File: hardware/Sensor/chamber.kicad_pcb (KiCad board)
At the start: 2 copper layers, 100 x 100 mm, 100 parts, among them J1 USB_B_Micro, J32 RF_Shield_Two_Pieces, J33 RF_Shield_Two_Pieces, J34 Conn_Coaxial, J51 Conn_02x05_Counter_Clockwise, J52 Conn_01x04, Q31 BC859, Q32 Q_NMOS_GDS, Q51 2N7002, Q52 Q_NPN_BEC, SW31 SW_DPDT_x2, SW32 SW_DPDT_x2, U31 MC34063AD, U32 LMC662, U33 LM358, U51 Opamp_Dual_Generic, U52 MCP3425A0T-ECH, U53 MCP3425A0T-ECH, U54 STM8S003F3P

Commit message: fix #64
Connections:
- J52 pad 2: /DataAcquisition/TX -> /DataAcquisition/RX
- J52 pad 3: /DataAcquisition/RX -> /DataAcquisition/TX
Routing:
- net /DataAcquisition/RX: track 14.9 -> 12.7 mm
- net /DataAcquisition/TX: track 9.60 -> 11.4 mm
- net /DataAcquisition/INT0: track 37.9 -> 37.0 mm
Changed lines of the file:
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@@
     (thickness 1.6)
     (drawings 19)
-    (tracks 665)
+    (tracks 668)
     (zones 0)
     (modules 100)
@@
   )
   (setup
-    (last_trace_width 0.3048)
+    (last_trace_width 0.254)
     (user_trace_width 0.254)
     (trace_clearance 0.254)
@@
       (net 1 GND))
     (pad 3 thru_hole oval (at 0 5.08 90) (size 1.7 1.7) (drill 1) (layers *.Cu *.Mask)
-      (net 47 /DataAcquisition/RX))
-    (pad 2 thru_hole oval (at 0 2.54 90) (size 1.7 1.7) (drill 1) (layers *.Cu *.Mask)
       (net 48 /DataAcquisition/TX))
+    (pad 2 thru_hole oval (at 0 2.54 90) (size 1.7 1.7) (drill 1) (layers *.Cu *.Mask)
+      (net 47 /DataAcquisition/RX))
     (pad 1 thru_hole rect (at 0 0 90) (size 1.7 1.7) (drill 1) (layers *.Cu *.Mask))
     (model ${KISYS3DMOD}/Connector_PinSocket_2.54mm.3dshapes/PinSocket_1x04_P2.54mm_Horizontal.wrl
@@
   (segment (start 126.286 134.331) (end 126.206 134.251) (width 0.3048) (layer F.Cu) (net 41) (status 30))
   (segment (start 130.466 134.331) (end 126.286 134.331) (width 0.3048) (layer F.Cu) (net 41) (status 30))
-  (segment (start 200.064001 135.993999) (end 200.914 135.144) (width 0.3048) (layer F.Cu) (net 42))
   (segment (start 184.0078 131.181) (end 184.767598 131.940798) (width 0.3048) (layer F.Cu) (net 42))
-  (segment (start 198.898 137.16) (end 200.064001 135.993999) (width 0.3048) (layer F.Cu) (net 42))
-  (segment (start 184.767598 131.940798) (end 184.767598 136.071074) (width 0.3048) (layer F.Cu) (net 42))
   (segment (start 182.978 131.181) (end 184.0078 131.181) (width 0.3048) (layer F.Cu) (net 42))
+  (segment (start 184.767598 131.940798) (end 184.767598 136.071074) (width 0.3048) (layer F.Cu) (net 42))
   (segment (start 184.767598 136.071074) (end 185.856524 137.16) (width 0.3048) (layer F.Cu) (net 42))
+  (segment (start 200.064001 135.993999) (end 200.914 135.144) (width 0.3048) (layer F.Cu) (net 42))
   (segment (start 185.856524 137.16) (end 198.898 137.16) (width 0.3048) (layer F.Cu) (net 42))
+  (segment (start 198.898 137.16) (end 200.064001 135.993999) (width 0.3048) (layer F.Cu) (net 42))
   (segment (start 197.2192 135.144) (end 198.374 135.144) (width 0.3048) (layer F.Cu) (net 43) (status 20))
   (segment (start 195.58 135.645) (end 196.587 135.645) (width 0.3048) (layer F.Cu) (net 43))
   (segment (start 197.088 135.144) (end 197.2192 135.144) (width 0.3048) (layer F.Cu) (net 43))
   (segment (start 196.587 135.645) (end 197.088 135.144) (width 0.3048) (layer F.Cu) (net 43))
-  (segment (start 194.265 136.16) (end 194.78 135.645) (width 0.3048) (layer F.Cu) (net 43))
-  (segment (start 189.992 136.16) (end 194.265 136.16) (width 0.3048) (layer F.Cu) (net 43))
-  (segment (start 194.78 135.645) (end 195.58 135.645) (width 0.3048) (layer F.Cu) (net 43))
-  (segment (start 188.878 130.531) (end 189.909522 130.531) (width 0.3048) (layer F.Cu) (net 43))
-  (segment (start 190.5 131.121478) (end 190.5 132.85) (width 0.3048) (layer F.Cu) (net 43))
+  (segment (start 194.956628 136.268372) (end 195.58 135.645) (width 0.3048) (layer F.Cu) (net 43))
+  (segment (start 189.9078 130.531) (end 190.5 131.1232) (width 0.3048) (layer F.Cu) (net 43))
+  (segment (start 188.878 130.531) (end 189.9078 130.531) (width 0.3048) (layer F.Cu) (net 43))
+  (segment (start 190.5 131.1232) (end 190.5 132.85) (width 0.3048) (layer F.Cu) (net 43))
+  (segment (start 190.100372 136.268372) (end 194.956628 136.268372) (width 0.3048) (layer F.Cu) (net 43))
   (segment (start 190.5 132.85) (end 189.016401 134.333599) (width 0.3048) (layer F.Cu) (net 43))
   (segment (start 189.016401 134.333599) (end 189.016401 135.184401) (width 0.3048) (layer F.Cu) (net 43))
-  (segment (start 189.909522 130.531) (end 190.5 131.121478) (width 0.3048) (layer F.Cu) (net 43))
-  (segment (start 189.016401 135.184401) (end 189.992 136.16) (width 0.3048) (layer F.Cu) (net 43))
+  (segment (start 189.016401 135.184401) (end 190.100372 136.268372) (width 0.3048) (layer F.Cu) (net 43))
   (segment (start 195.834 127.524) (end 198.374 130.064) (width 0.3048) (layer F.Cu) (net 44) (status 20))
   (segment (start 191.77 127.016) (end 192.278 127.524) (width 0.3048) (layer F.Cu) (net 44))
@@
   (segment (start 190.653 127.931) (end 191.77 129.048) (width 0.3048) (layer F.Cu) (net 46) (status 20))
   (segment (start 188.878 127.931) (end 190.653 127.931) (width 0.3048) (layer F.Cu) (net 46) (status 10))
-  (via (at 187.96 136.144) (size 1) (drill 0.5) (layers F.Cu B.Cu) (net 47))
-  (segment (start 186.944 136.144) (end 187.96 136.144) (width 0.3048) (layer F.Cu) (net 47))
-  (segment (start 185.674 134.874) (end 186.944 136.144) (width 0.3048) (layer F.Cu) (net 47))
-  (segment (start 185.674 132.334) (end 185.674 134.874) (width 0.3048) (layer F.Cu) (net 47))
+  (via (at 186.436 135.636) (size 1) (drill 0.5) (layers F.Cu B.Cu) (net 47))
+  (segment (start 185.42 134.62) (end 186.436 135.636) (width 0.3048) (layer F.Cu) (net 47))
+  (segment (start 185.42 132.588) (end 185.42 134.62) (width 0.3048) (layer F.Cu) (net 47))
   (segment (start 188.878 131.181) (end 186.827 131.181) (width 0.3048) (layer F.Cu) (net 47))
-  (segment (start 186.827 131.181) (end 185.674 132.334) (width 0.3048) (layer F.Cu) (net 47))
-  (segment (start 188.459999 136.643999) (end 190.745999 136.643999) (width 0.254) (layer B.Cu) (net 47))
-  (segment (start 187.96 136.144) (end 188.459999 136.643999) (width 0.254) (layer B.Cu) (net 47))
-  (segment (start 190.745999 136.643999) (end 191.77 137.668) (width 0.254) (layer B.Cu) (net 47))
-  (segment (start 191.77 137.668) (end 191.77 139.065) (width 0.254) (layer B.Cu) (net 47))
-  (via (at 186.926029 133.025499) (size 1) (drill 0.5) (layers F.Cu B.Cu) (net 48))
+  (segment (start 186.827 131.181) (end 185.42 132.588) (width 0.3048) (layer F.Cu) (net 47))
+  (segment (start 187.452 136.652) (end 186.436 135.636) (width 0.254) (layer B.Cu) (net 47))
+  (segment (start 188.468 136.652) (end 187.452 136.652) (width 0.254) (layer B.Cu) (net 47))
+  (segment (start 189.23 139.065) (end 189.23 137.414) (width 0.254) (layer B.Cu) (net 47))
+  (segment (start 189.23 137.414) (end 188.468 136.652) (width 0.254) (layer B.Cu) (net 47))
+  (via (at 187.96 135.636) (size 1) (drill 0.5) (layers F.Cu B.Cu) (net 48))
+  (segment (start 186.436007 133.243193) (end 186.436007 133.404894) (width 0.3048) (layer F.Cu) (net 48))
+  (segment (start 186.436007 133.404894) (end 186.436007 134.112) (width 0.3048) (layer F.Cu) (net 48))
+  (segment (start 187.8482 131.831) (end 186.436007 133.243193) (width 0.3048) (layer F.Cu) (net 48))
   (segment (start 188.878 131.831) (end 187.8482 131.831) (width 0.3048) (layer F.Cu) (net 48))
-  (segment (start 186.926029 132.753171) (end 186.926029 133.025499) (width 0.3048) (layer F.Cu) (net 48))
-  (segment (start 187.8482 131.831) (end 186.926029 132.753171) (width 0.3048) (layer F.Cu) (net 48))
-  (segment (start 186.926029 136.761029) (end 186.926029 133.732605) (width 0.254) (layer B.Cu) (net 48))
-  (segment (start 189.23 139.065) (end 186.926029 136.761029) (width 0.254) (layer B.Cu) (net 48))
-  (segment (start 186.926029 133.732605) (end 186.926029 133.025499) (width 0.254) (layer B.Cu) (net 48))
+  (segment (start 186.436007 134.112007) (end 187.96 135.636) (width 0.254) (layer F.Cu) (net 48))
+  (segment (start 186.436007 134.112) (end 186.436007 134.112007) (width 0.254) (layer F.Cu) (net 48))
+  (segment (start 191.77 138.938) (end 191.77 139.065) (width 0.254) (layer B.Cu) (net 48))
+  (segment (start 187.96 135.636) (end 188.468 135.636) (width 0.254) (layer B.Cu) (net 48))
+  (segment (start 188.468 135.636) (end 191.77 138.938) (width 0.254) (layer B.Cu) (net 48))
   (segment (start 184.64 125.746) (end 184.64 128.141) (width 0.3048) (layer F.Cu) (net 49))
   (segment (start 186.38 129.881) (end 188.878 129.881) (width 0.3048) (layer F.Cu) (net 49) (status 20))
@@
   (segment (start 184.66829 110.64329) (end 185.361361 111.336361) (width 0.3048) (layer F.Cu) (net 50))
   (segment (start 185.361361 111.336361) (end 185.361361 111.369869) (width 0.3048) (layer F.Cu) (net 50))
-  (segment (start 192.405 115.84) (end 192.405 129.683) (width 0.3048) (layer B.Cu) (net 50))
-  (segment (start 192.405 129.683) (end 187.96 134.128) (width 0.3048) (layer B.Cu) (net 50))
-  (segment (start 188.878 133.21) (end 187.96 134.128) (width 0.3048) (layer F.Cu) (net 50))
-  (segment (start 185.361361 111.369869) (end 187.934869 111.369869) (width 0.3048) (layer B.Cu) (net 50))
-  (segment (start 188.878 132.481) (end 188.878 133.21) (width 0.3048) (layer F.Cu) (net 50) (status 10))
-  (via (at 187.96 134.128) (size 1) (drill 0.5) (layers F.Cu B.Cu) (net 50))
-  (segment (start 187.934869 111.369869) (end 192.405 115.84) (width 0.3048) (layer B.Cu) (net 50))
   (segment (start 185.101 105.101) (end 185.157 105.045) (width 0.254) (layer F.Cu) (net 50) (status 30))
+  (segment (start 188.878 133.0108) (end 188.284798 133.604002) (width 0.3048) (layer F.Cu) (net 50))
+  (segment (start 192.405 115.84) (end 192.405 129.159002) (width 0.3048) (layer B.Cu) (net 50))
+  (segment (start 188.284798 133.604002) (end 187.96 133.604002) (width 0.3048) (layer F.Cu) (net 50))
+  (segment (start 187.934869 111.369869) (end 192.405 115.84) (width 0.3048) (layer B.Cu) (net 50))
+  (segment (start 192.405 129.159002) (end 188.459999 133.104003) (width 0.3048) (layer B.Cu) (net 50))
+  (segment (start 188.459999 133.104003) (end 187.96 133.604002) (width 0.3048) (layer B.Cu) (net 50))
+  (segment (start 188.878 132.481) (end 188.878 133.0108) (width 0.3048) (layer F.Cu) (net 50))
+  (via (at 187.96 133.604002) (size 1) (drill 0.5) (layers F.Cu B.Cu) (net 50))
+  (segment (start 185.361361 111.369869) (end 187.934869 111.369869) (width 0.3048) (layer B.Cu) (net 50))
   (segment (start 188.878 125.082) (end 189.484 124.476) (width 0.3048) (layer F.Cu) (net 51) (status 20))
   (segment (start 188.878 126.631) (end 188.878 125.082) (width 0.3048) (layer F.Cu) (net 51) (status 10))

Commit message: fix #197
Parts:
- C46: value 2p2 -> not mounted
- C47, C48: value C -> 0R resistor
- R38: value 4*100G -> 2*50G
- R39, R41: value R -> 10k
- R40: value R -> 120k
- R42: value R -> 22k
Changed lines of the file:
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@@
       (effects (font (size 1 1) (thickness 0.15)) (justify mirror))
     )
-    (fp_text value C (at 0 -1.65 180) (layer B.Fab)
+    (fp_text value "0R resistor" (at 0 -1.65 180) (layer B.Fab)
       (effects (font (size 1 1) (thickness 0.15)) (justify mirror))
     )
@@
       (effects (font (size 1 1) (thickness 0.15)) (justify mirror))
     )
-    (fp_text value R (at 0 -1.65) (layer B.Fab)
+    (fp_text value 22k (at 0 -1.65) (layer B.Fab)
       (effects (font (size 1 1) (thickness 0.15)) (justify mirror))
     )
@@
       (effects (font (size 1 1) (thickness 0.15)) (justify mirror))
     )
-    (fp_text value R (at 0 -1.65 270) (layer B.Fab)
+    (fp_text value 10k (at 0 -1.65 270) (layer B.Fab)
       (effects (font (size 1 1) (thickness 0.15)) (justify mirror))
     )
@@
       (effects (font (size 1 1) (thickness 0.15)) (justify mirror))
     )
-    (fp_text value C (at 0 -1.65) (layer B.Fab)
+    (fp_text value "0R resistor" (at 0 -1.65) (layer B.Fab)
       (effects (font (size 1 1) (thickness 0.15)) (justify mirror))
     )
@@
       (effects (font (size 1 1) (thickness 0.15)) (justify mirror))
     )
-    (fp_text value 2p2 (at 0 -1.65 270) (layer B.Fab)
+    (fp_text value "not mounted" (at 0 -1.65 270) (layer B.Fab)
       (effects (font (size 1 1) (thickness 0.15)) (justify mirror))
     )
@@
       (effects (font (size 1 1) (thickness 0.15)) (justify mirror))
     )
-    (fp_text value R (at 0 -1.65 270) (layer B.Fab)
+    (fp_text value 120k (at 0 -1.65 270) (layer B.Fab)
       (effects (font (size 1 1) (thickness 0.15)) (justify mirror))
     )
@@
       (effects (font (size 1 1) (thickness 0.15)) (justify mirror))
     )
-    (fp_text value R (at 0 -1.65 270) (layer B.Fab)
+    (fp_text value 10k (at 0 -1.65 270) (layer B.Fab)
       (effects (font (size 1 1) (thickness 0.15)) (justify mirror))
     )
@@
       (effects (font (size 1 1) (thickness 0.15)) (justify mirror))
     )
-    (fp_text value 4*100G (at 0 -1.65 270) (layer B.Fab)
-      (effects (font (size 1 1) (thickness 0.15)) (justify mirror))
-    )
+    (fp_text value 2*50G (at 0 -1.65 270) (layer B.Fab)
+      (effects (font (size 1 1) (thickness 0.15)) (justify mirror))
+    )

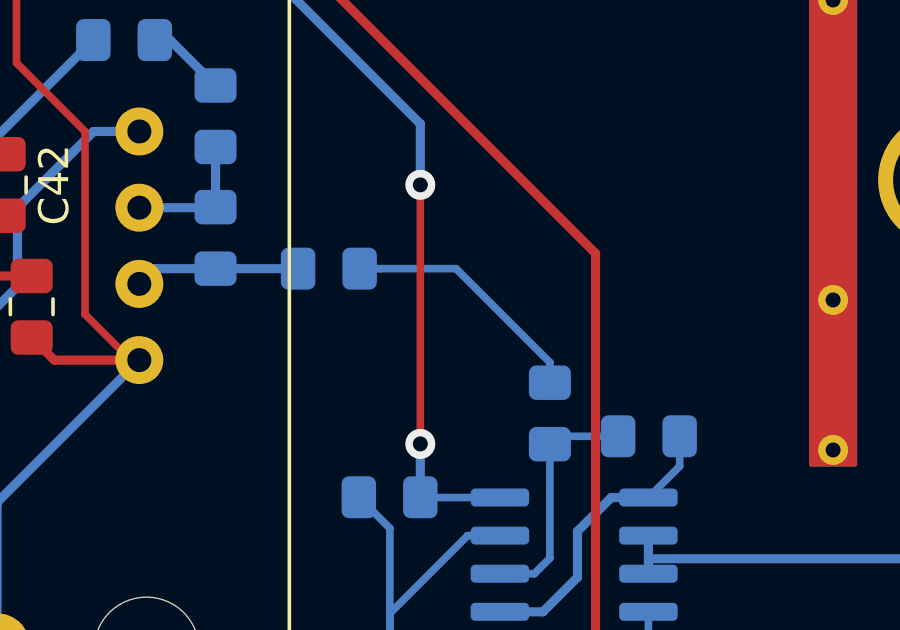
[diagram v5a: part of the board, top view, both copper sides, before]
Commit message: fix #211
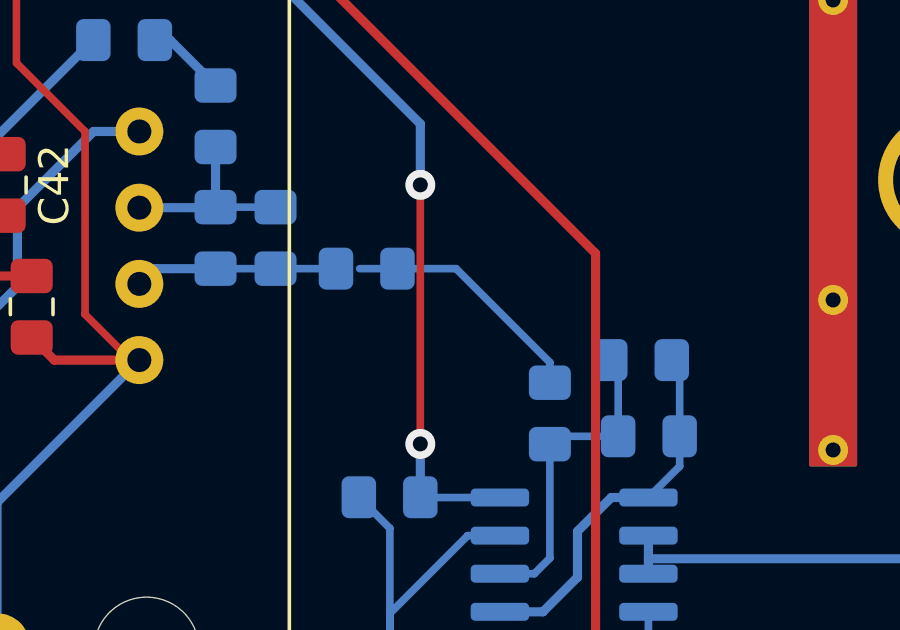
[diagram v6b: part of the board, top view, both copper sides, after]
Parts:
- added C4: 0R resistor, Capacitor_SMD:C_0805_2012Metric_Pad1.15x1.40mm_HandSolder, B.Cu at (174.2, 69.6)
- added C5: 0R resistor, Capacitor_SMD:C_0805_2012Metric_Pad1.15x1.40mm_HandSolder, B.Cu at (186.4, 73.7)
- moved C48 1.26 mm to (177.3, 70.6)
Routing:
- net Net-(C5-Pad2): track 9.90 -> 12.5 mm
- net Net-(C5-Pad1): track 8.07 -> 10.7 mm
- net Net-(C4-Pad1): track 4.55 -> 6.55 mm
- net Net-(C4-Pad2): track 5.50 -> 6.76 mm
- net Net-(C48-Pad2): track 8.31 -> 7.72 mm
